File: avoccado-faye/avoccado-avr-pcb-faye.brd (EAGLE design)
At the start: 25 x 24.5 mm, 55 parts, among them Q1 16MHz, Q2 FET, U2 MCP73831

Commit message: pour top GND polygon
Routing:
- net 3.3V: track 81.0 -> 86.2 mm
- net GND: track 104.1 -> 105.2 mm, vias 3 -> 9
- added copper zone on layer 1, net GND
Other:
- board text added: "AVOCCADO° FAYE SHURE OPEN TECHNOLOGIES ETEMU.COM 2015"
- board text removed: "AVOCCADO NORA 2 SHURE OPEN TECHNOLOGIES ETEMU.COM 2015"

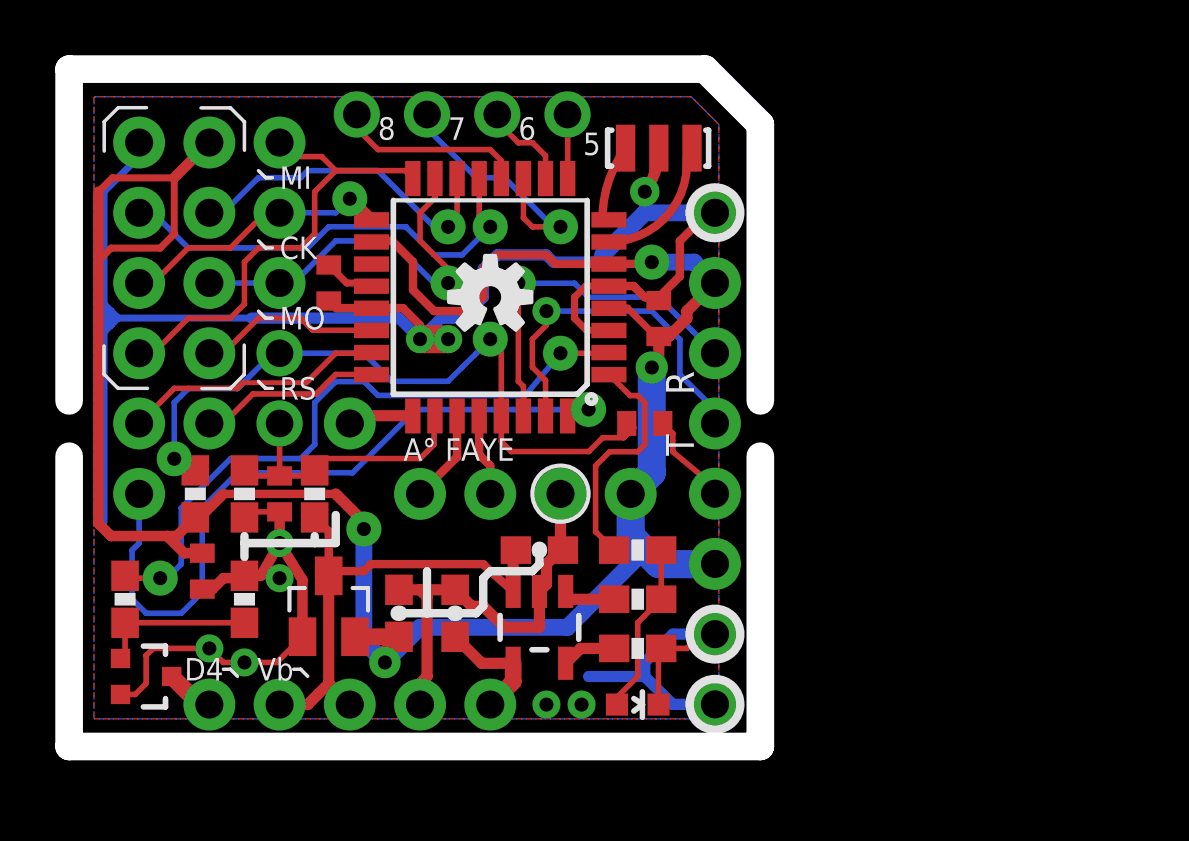
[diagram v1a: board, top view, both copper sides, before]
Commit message: change footprint of mosfet to sot23-3
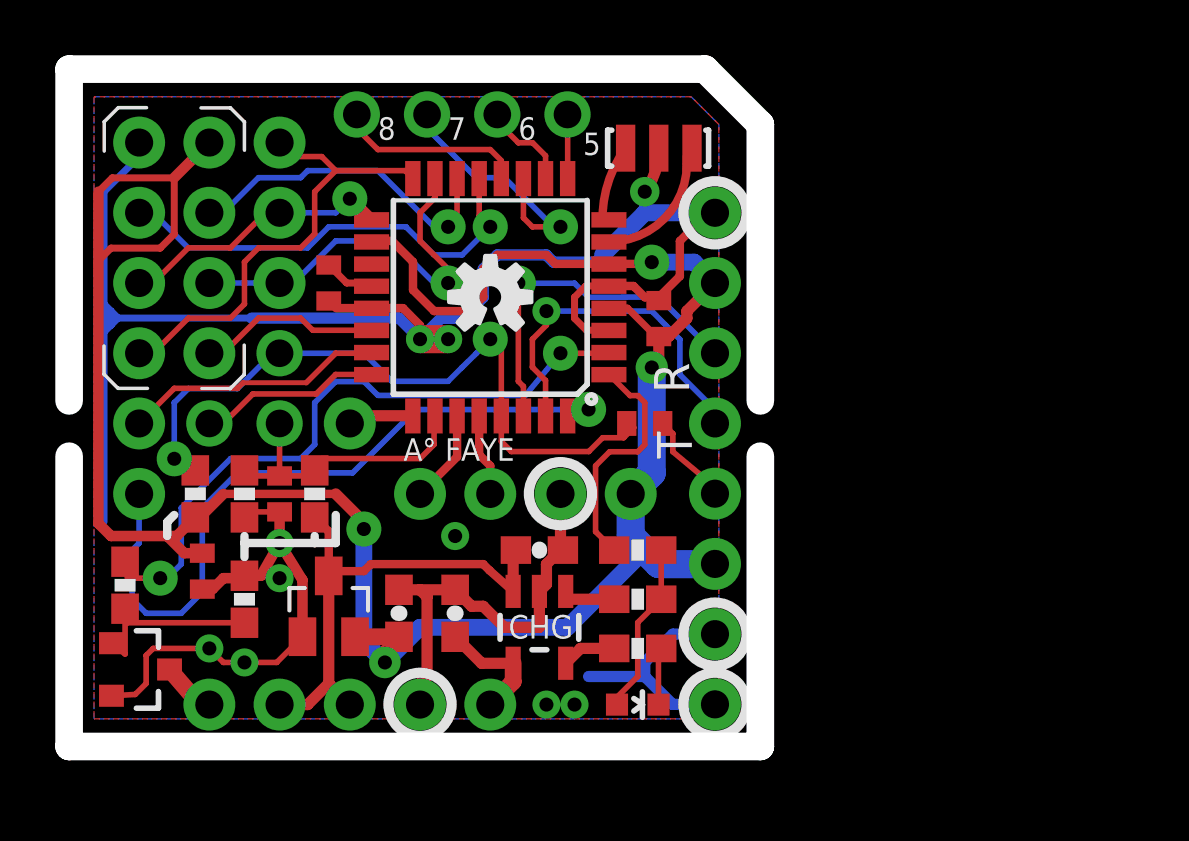
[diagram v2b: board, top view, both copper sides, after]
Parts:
- JP20: value M01PTH -> M01NOSILK-KIT; device SparkFun-Connectors:1X01 -> SparkFun-Connectors:1X01NS-KIT
- Q2: device SparkFun-DiscreteSemi:SOT323 -> SparkFun-DiscreteSemi:SOT23-3
- moved R1 0.51 mm to (1.52, 5.33)
- moved Q2 0.36 mm to (2.03, 2.29)
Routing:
- net GND: track 105.2 -> 103.3 mm, vias 9 -> 10
- net N$6: track 5.68 -> 6.62 mm
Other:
- board text added: "CHG"

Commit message: bigger pads for test jig, g-code for solder stencils
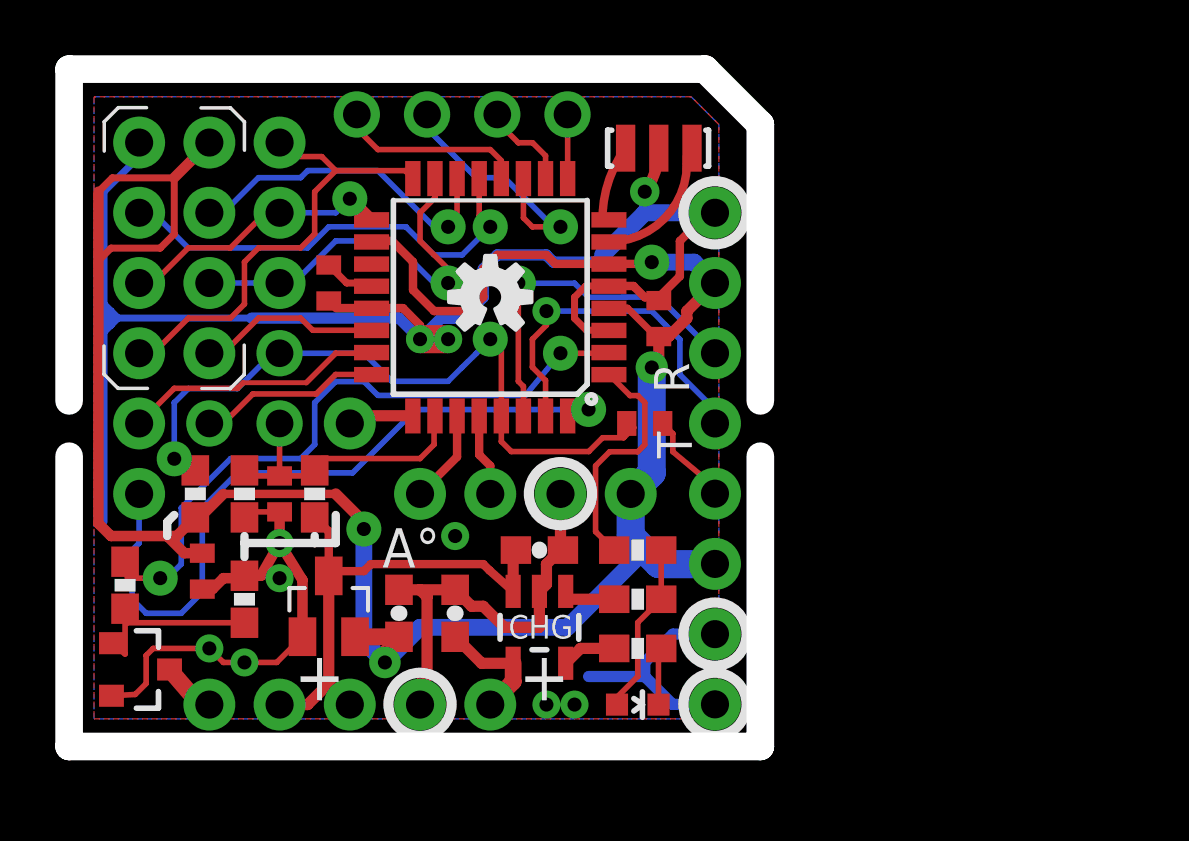
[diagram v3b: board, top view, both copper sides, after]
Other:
- board text added: "A°"
- board text added: "Vin"
- board text removed: "A° FAYE"
- board text removed: "NRF24L01+"
- board text removed: "Vi"

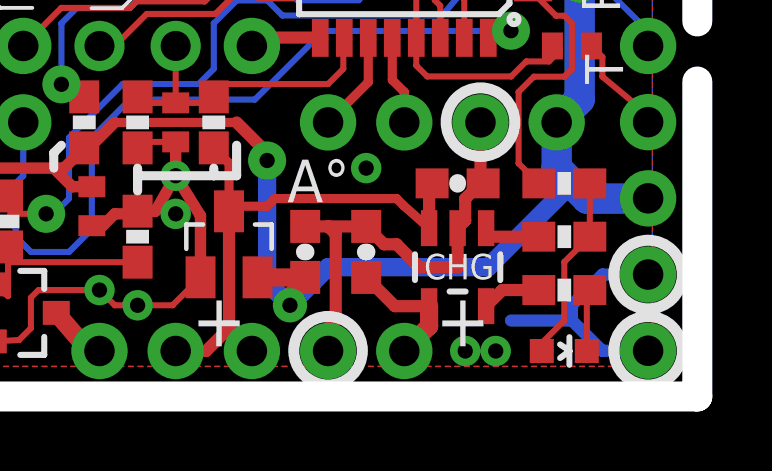
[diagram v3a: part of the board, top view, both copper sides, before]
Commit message: micro usb on the bottom
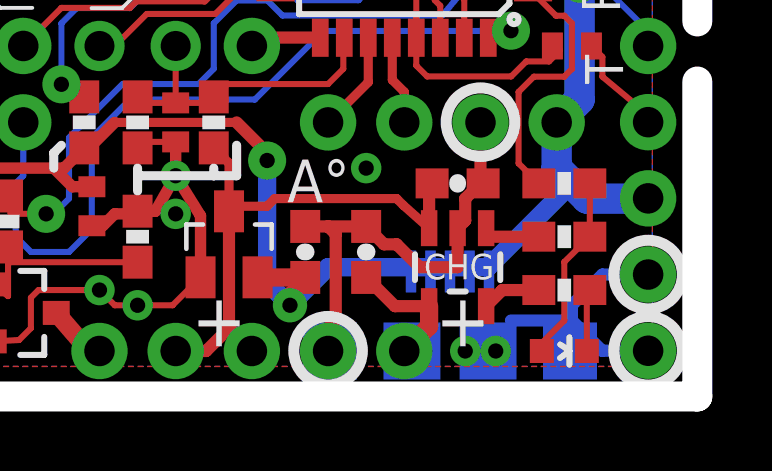
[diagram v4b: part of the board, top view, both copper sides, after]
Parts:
- added JP7: USB-MICROB, SparkFun-Connectors:USB-MICROB
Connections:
- net 5V: now also JP7.VBUS
- net GND: now also JP7.GND, JP7.MT1, JP7.MT2
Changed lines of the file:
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@@
 <setting verticaltext="up"/>
 </settings>
-<grid distance="1" unitdist="mm" unit="mm" style="lines" multiple="1" display="yes" altdistance="0.1" altunitdist="mm" altunit="mm"/>
+<grid distance="0.02" unitdist="inch" unit="inch" style="lines" multiple="1" display="yes" altdistance="0.01" altunitdist="inch" altunit="inch"/>
 <layers>
-<layer number="1" name="Top" color="5" fill="1" visible="no" active="yes"/>
+<layer number="1" name="Top" color="5" fill="1" visible="yes" active="yes"/>
 <layer number="2" name="Route2" color="1" fill="3" visible="no" active="no"/>
 <layer number="3" name="Route3" color="4" fill="3" visible="no" active="no"/>
@@
 <layer number="14" name="Route14" color="1" fill="6" visible="no" active="no"/>
 <layer number="15" name="Route15" color="4" fill="6" visible="no" active="no"/>
-<layer number="16" name="Bottom" color="1" fill="1" visible="no" active="yes"/>
-<layer number="17" name="Pads" color="14" fill="1" visible="no" active="yes"/>
+<layer number="16" name="Bottom" color="1" fill="1" visible="yes" active="yes"/>
+<layer number="17" name="Pads" color="14" fill="1" visible="yes" active="yes"/>
 <layer number="18" name="Vias" color="6" fill="1" visible="yes" active="yes"/>
-<layer number="19" name="Unrouted" color="6" fill="1" visible="no" active="yes"/>
-<layer number="20" name="Dimension" color="15" fill="1" visible="no" active="yes"/>
+<layer number="19" name="Unrouted" color="6" fill="1" visible="yes" active="yes"/>
+<layer number="20" name="Dimension" color="15" fill="1" visible="yes" active="yes"/>
 <layer number="21" name="tPlace" color="15" fill="1" visible="yes" active="yes"/>
 <layer number="22" name="bPlace" color="6" fill="1" visible="yes" active="yes"/>
-<layer number="23" name="tOrigins" color="15" fill="1" visible="no" active="yes"/>
-<layer number="24" name="bOrigins" color="15" fill="1" visible="no" active="yes"/>
+<layer number="23" name="tOrigins" color="15" fill="1" visible="yes" active="yes"/>
+<layer number="24" name="bOrigins" color="15" fill="1" visible="yes" active="yes"/>
 <layer number="25" name="tNames" color="7" fill="1" visible="no" active="yes"/>
 <layer number="26" name="bNames" color="7" fill="1" visible="no" active="yes"/>
 <layer number="27" name="tValues" color="7" fill="1" visible="no" active="yes"/>
 <layer number="28" name="bValues" color="7" fill="1" visible="no" active="yes"/>
-<layer number="29" name="tStop" color="7" fill="3" visible="yes" active="yes"/>
+<layer number="29" name="tStop" color="7" fill="3" visible="no" active="yes"/>
 <layer number="30" name="bStop" color="7" fill="6" visible="no" active="yes"/>
-<layer number="31" name="tCream" color="7" fill="4" visible="yes" active="yes"/>
+<layer number="31" name="tCream" color="7" fill="4" visible="no" active="yes"/>
 <layer number="32" name="bCream" color="7" fill="5" visible="no" active="yes"/>
 <layer number="33" name="tFinish" color="6" fill="3" visible="no" active="yes"/>
@@
 <layer number="43" name="vRestrict" color="2" fill="10" visible="no" active="yes"/>
 <layer number="44" name="Drills" color="7" fill="1" visible="no" active="yes"/>
-<layer number="45" name="Holes" color="7" fill="1" visible="no" active="yes"/>
+<layer number="45" name="Holes" color="7" fill="1" visible="yes" active="yes"/>
 <layer number="46" name="Milling" color="3" fill="1" visible="no" active="yes"/>
 <layer number="47" name="Measures" color="7" fill="1" visible="no" active="yes"/>
@@
 <layer number="49" name="Reference" color="7" fill="1" visible="no" active="yes"/>
 <layer number="50" name="dxf" color="7" fill="1" visible="no" active="yes"/>
-<layer number="51" name="tDocu" color="6" fill="1" visible="no" active="yes"/>
+<layer number="51" name="tDocu" color="6" fill="1" visible="yes" active="yes"/>
 <layer number="52" name="bDocu" color="7" fill="1" visible="no" active="yes"/>
 <layer number="53" name="tGND_GNDA" color="7" fill="9" visible="no" active="no"/>
@@
 <attribute name="PROD_ID" value="IC-09069" x="14.732" y="15.748" size="1.778" layer="27" font="vector" ratio="15" rot="R180" display="off"/>
 </element>
+<element name="JP7" library="SparkFun-Connectors" package="USB-MICROB" value="USB-MICROB" x="16.256" y="1.016" rot="MR0">
+<attribute name="PROD_ID" value="CONN-09505" x="16.256" y="1.016" size="1.778" layer="28" font="vector" ratio="15" rot="MR0" display="off"/>
+</element>
 </elements>
 <signals>
@@
 <wire x1="12.192" y1="14.232" x2="13.208" y2="14.232" width="1.016" layer="1"/>
 <via x="13.462" y="7.112" extent="1-16" drill="0.508" diameter="1.016"/>
-<wire x1="19.0246" y1="14.556" x2="19.0246" y2="14.548" width="0" layer="19" extent="1-1"/>
+<contactref element="JP7" pad="GND"/>
+<contactref element="JP7" pad="MT2"/>
+<contactref element="JP7" pad="MT1"/>
+<wire x1="19.0246" y1="16.156" x2="19.0246" y2="16.148" width="0" layer="19" extent="1-1"/>
+<wire x1="19.0246" y1="14.548" x2="19.0246" y2="14.556" width="0" layer="19" extent="1-1"/>
 <wire x1="10.4394" y1="15.348" x2="11.43" y2="14.994" width="0" layer="19" extent="1-16"/>
+<wire x1="4.318" y1="5.192" x2="0.762" y2="7.628" width="0" layer="19" extent="1-16"/>
+<wire x1="7.112" y1="5.588" x2="6.438" y2="5.676" width="0" layer="19" extent="1-1"/>
+<wire x1="5.842" y1="2.54" x2="5.08" y2="2.54" width="0" layer="19" extent="1-1"/>
+<wire x1="11.43" y1="5.168" x2="7.94" y2="5.522" width="0" layer="19" extent="1-1"/>
+<wire x1="13.462" y1="7.112" x2="13.462" y2="5.168" width="0" layer="19" extent="1-1"/>
+<wire x1="18.288" y1="2.032" x2="16.51" y2="3.81" width="0" layer="19" extent="1-16"/>
+<wire x1="22.86" y1="3.564" x2="22.848" y2="3.564" width="0" layer="19" extent="16-16"/>
+<wire x1="20.816" y1="1.016" x2="21.328" y2="1.024" width="0" layer="19" extent="1-16"/>
+<wire x1="17.78" y1="1.016" x2="18.288" y2="2.032" width="0" layer="19" extent="16-16"/>
+<wire x1="16.764" y1="1.016" x2="17.78" y2="1.016" width="0" layer="19" extent="1-1"/>
+<wire x1="14.956" y1="3.666" x2="1.89" y2="1.382" width="0" layer="19" extent="1-1"/>
+<wire x1="12.256" y1="1.016" x2="14.956" y2="3.666" width="0" layer="19" extent="1-1"/>
+<wire x1="20.256" y1="1.016" x2="14.956" y2="3.666" width="0" layer="19" extent="1-1"/>
 </signal>
 <signal name="AREF">
@@
 <wire x1="13.6581" y1="3.2719" x2="14.4201" y2="2.5099" width="0.4064" layer="1"/>
 <wire x1="14.4201" y1="2.5099" x2="15.56" y2="2.5099" width="0.4064" layer="1"/>
+<contactref element="JP7" pad="VBUS"/>
+<wire x1="17.556" y1="3.666" x2="14.732" y2="1.016" width="0" layer="19" extent="1-1"/>
 </signal>
 <signal name="SOC">

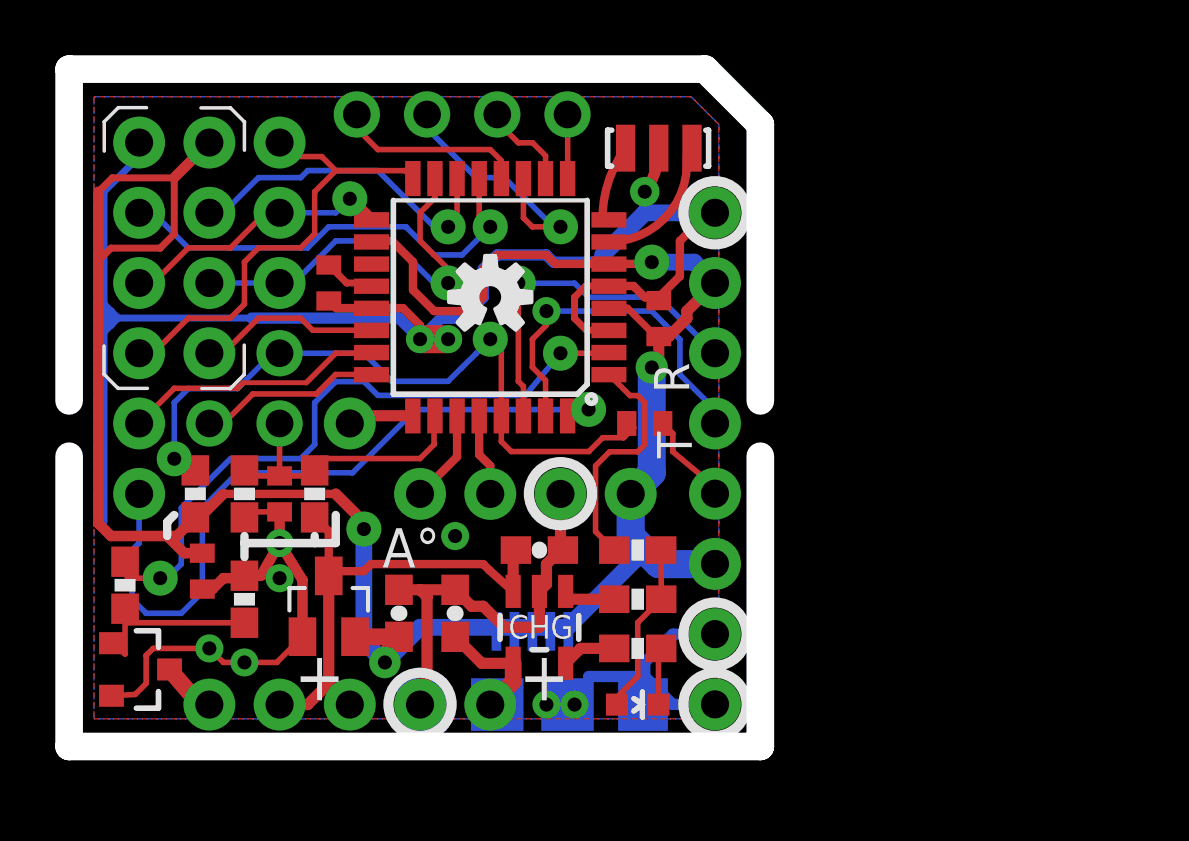
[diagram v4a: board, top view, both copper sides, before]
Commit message: route USB connector, additional headers
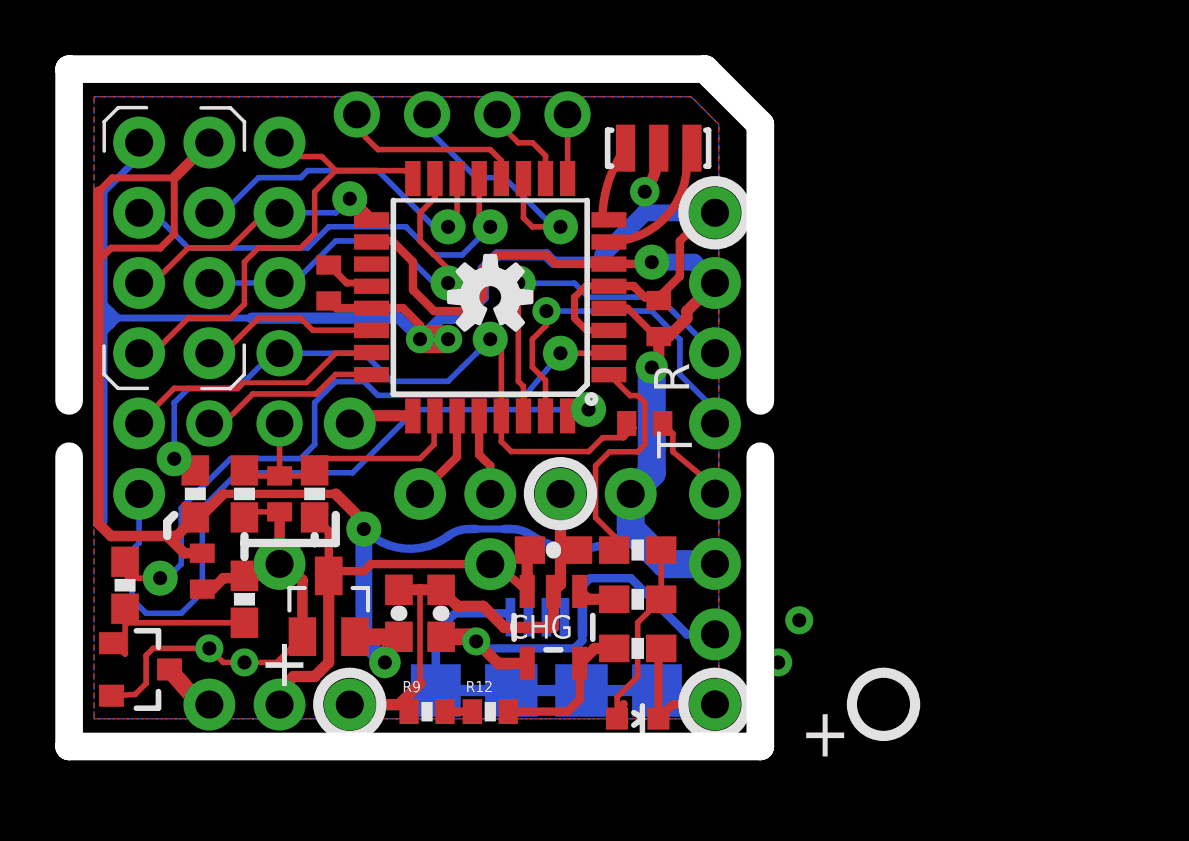
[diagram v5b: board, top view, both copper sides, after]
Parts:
- added R12, R9: 1K, SparkFun-Resistors:0402-RES
- moved JP6 16.0 mm to (7.11, 6.10)
- moved JP17 8.52 mm to (22.9, 3.56)
- moved JP1 7.18 mm to (14.7, 6.10)
- moved JP25 2.54 mm to (9.65, 1.02)
- moved JP7 0.72 mm to (16.8, 1.52)
- moved D1 0.51 mm to (20.1, 0.51)
- moved C4 0.51 mm to (13.0, 4.32)
- moved C5 0.51 mm to (17.0, 6.60)
- moved U2 0.51 mm to (17.0, 3.81)
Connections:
- new net N$3: R12.1, R9.2
- net CHG-PROG: now also R12.2
- net GND: now also R9.1
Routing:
- net GND: track 103.3 -> 121.1 mm, vias 10 -> 7
- net 5V: track 4.33 -> 15.3 mm, vias 0 -> 1
- net CHG-PROG: track 1.98 -> 5.55 mm
- net 3.3V: track 86.2 -> 84.7 mm
- net N$3: track 0.00 -> 0.99 mm
- net LED: track 6.49 -> 7.34 mm
- net VBAT: track 18.4 -> 17.7 mm
- net SOC: track 2.01 -> 1.37 mm
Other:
- board text removed: "3.3V 3.6-4.2V 5-5.5V"
- board text removed: "A1"
- board text removed: "A3"
- board text removed: "AO"
- board text removed: "A°"
- board text removed: "MPU6050"
- board text removed: "Vc Vb Vi"
